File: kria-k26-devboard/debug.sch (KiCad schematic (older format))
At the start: 70 parts, among them J8 USB4105-GF-A, J9 0878311420, Q10 BSS138-7-F, Q11 BSS138-7-F, Q17 DTC014TEBTL, Q9 BSS138-7-F, U28 WE-TVS-82400152, U29 MIC5211-3.3YM6-TR, U30 FT4232HPQ, U31 93LC56CT-IMC, U32 74AVC4T245RSVRG4, U33 74AVC4T245RSVRG4, U34 SN74AVC2T245RSWR, U35 SN74AVC2T245RSWR, U36 NC7WZ07P6X, U54 TPD4E05U06QDQARQ1, Y5 ABM8G-12.000MHZ-18-D2Y-T

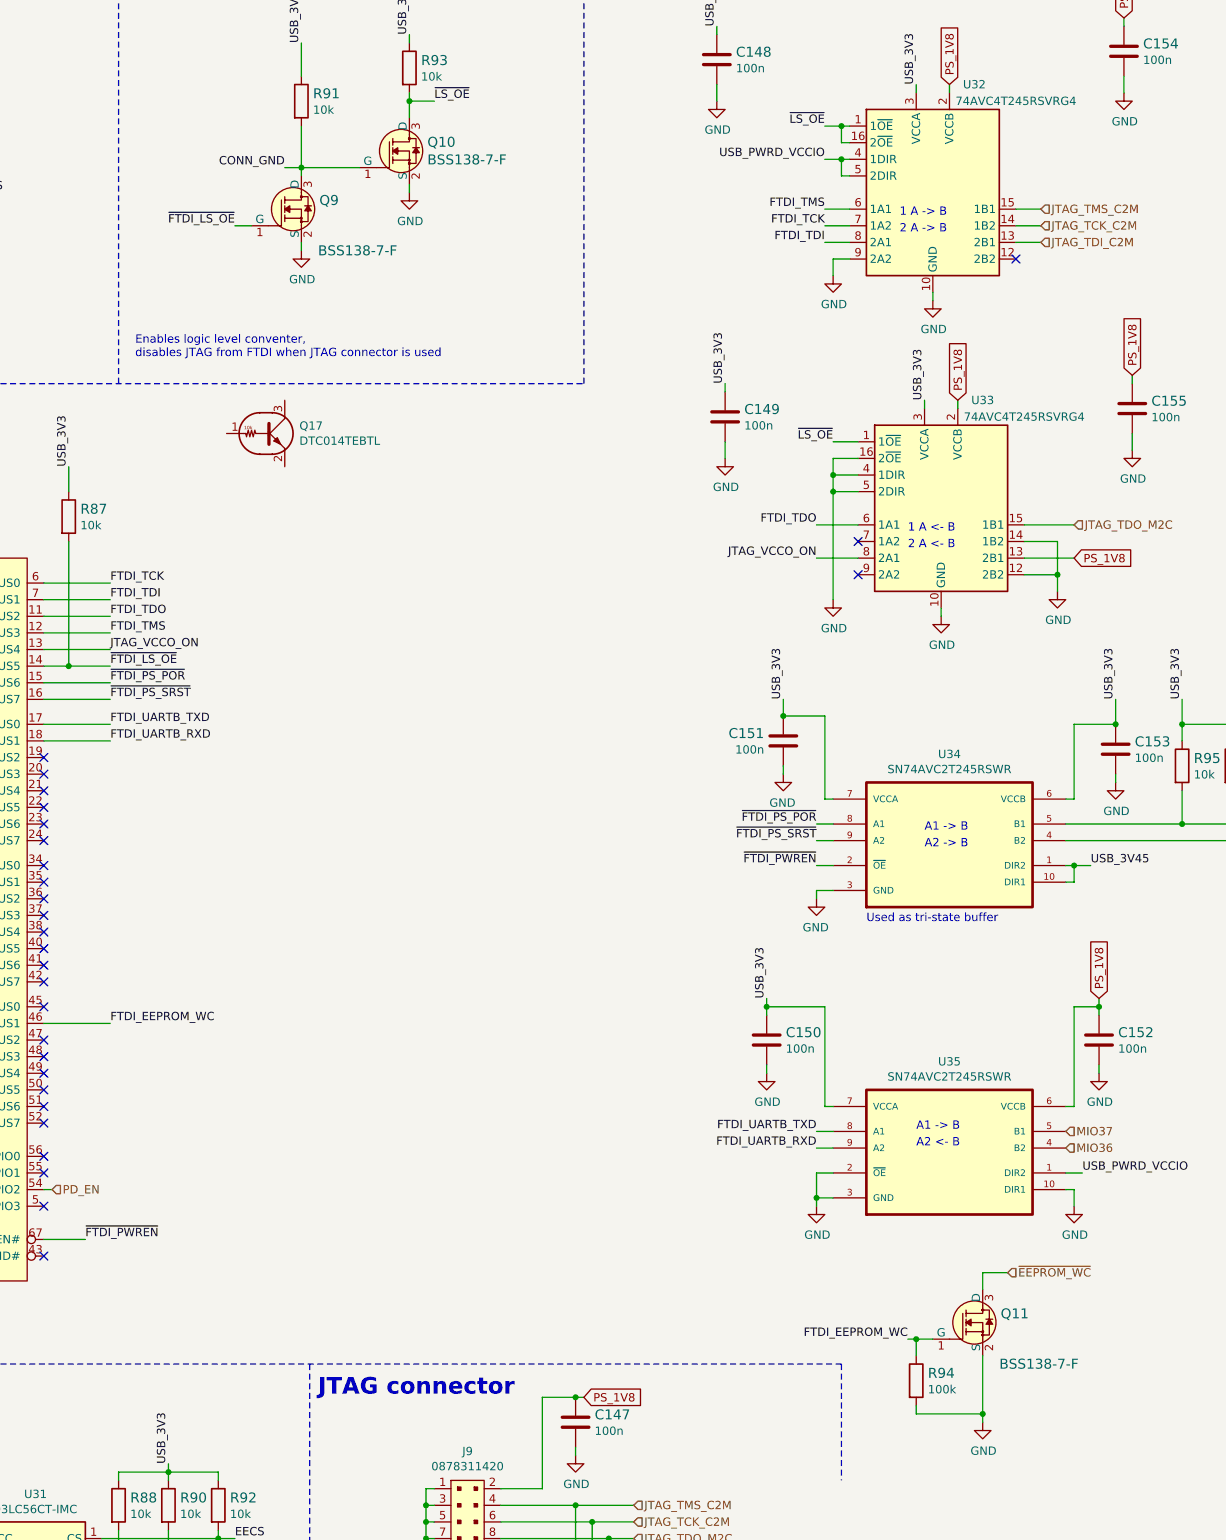
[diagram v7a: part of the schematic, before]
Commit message: Routed PS reset, improved SOM fanout, routed remaing SD 3.0 traces, component size optimization
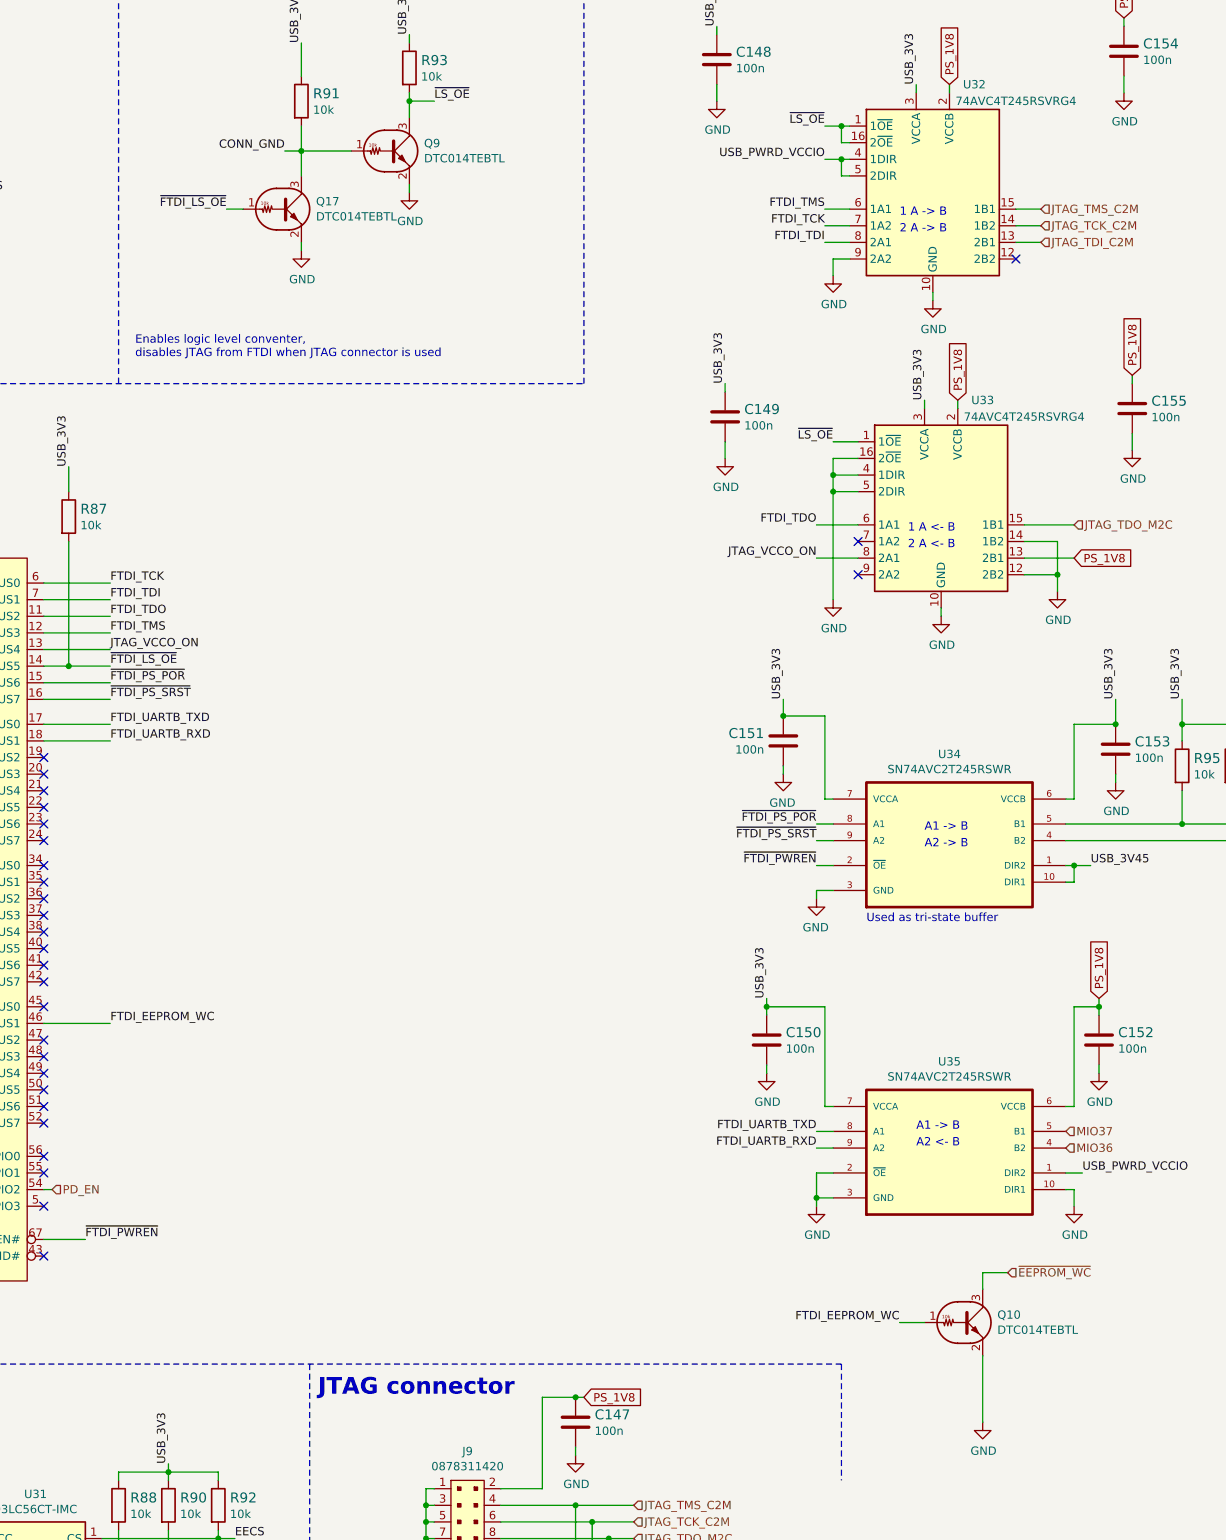
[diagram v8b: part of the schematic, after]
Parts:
- removed Q10, Q11, Q9: BSS138-7-F, antmicro-footprints:SOT-23-3, symbol antmicroTransistorsFETsMOSFETsSingle:BSS138-7-F
- removed R94: R_100k_0402, antmicro-footprints:0402-res, symbol antmicroResistors0402:R_100k_0402
- added Q10, Q9: DTC014TEBTL, antmicro-footprints:SOT-416, symbol antmicroTransistorsBipolarSingle:DTC014TEBTL
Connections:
- net CONN_GND: now also Q17.3 (C), Q9.1 (B)
- net FTDI_EEPROM_WC: now also Q10.1 (B)
- net GND: now also Q17.2 (E), Q10.2 (E), Q9.2 (E)
- net ~EEPROM_WC: now also Q10.3 (C)
- net ~FTDI_LS_OE: now also Q17.1 (B)
- net ~LS_OE: now also Q9.3 (C)
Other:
- moved on the sheet: Q17
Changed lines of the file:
@@
 FTDI_TMS
-$Comp
-L antmicroTransistorsFETsMOSFETsSingle:BSS138-7-F Q9
-U 1 1 623BDEBC
-P 8550 2300
-F 0 "Q9" H 8658 2353 60  0000 L CNN
-F 1 "BSS138-7-F" H 8650 2050 60  0000 L CNN
-F 2 "antmicro-footprints:SOT-23-3" H 8750 2500 60  0001 L CNN
-F 3 "https://www.diodes.com/assets/Datasheets/ds30144.pdf" H 8750 2600 60  0001 L CNN
-F 4 "BSS138-7-F" H 8750 2800 60  0001 L CNN "MPN"
-F 5 "Diodes Incorporated" H 8750 3400 60  0001 L CNN "Manufacturer"
-	1    8550 2300
-	1    0    0    -1
-$EndComp
 $Comp
 L antmicroResistors0402:R_10k_0402 R91
@@
 $EndComp
 $Comp
-L antmicroTransistorsFETsMOSFETsSingle:BSS138-7-F Q10
-U 1 1 623C3158
-P 9200 1950
-F 0 "Q10" H 9308 2003 60  0000 L CNN
-F 1 "BSS138-7-F" H 9308 1897 60  0000 L CNN
-F 2 "antmicro-footprints:SOT-23-3" H 9400 2150 60  0001 L CNN
-F 3 "https://www.diodes.com/assets/Datasheets/ds30144.pdf" H 9400 2250 60  0001 L CNN
-F 4 "BSS138-7-F" H 9400 2450 60  0001 L CNN "MPN"
-F 5 "Diodes Incorporated" H 9400 3050 60  0001 L CNN "Manufacturer"
-	1    9200 1950
-	1    0    0    -1
-$EndComp
-$Comp
 L antmicroResistors0402:R_10k_0402 R93
 U 1 1 623C4098
@@
 $EndComp
 Wire Wire Line
-	8550 2100 8550 2050
+	8550 2100 8550 1950
 Wire Wire Line
 	9200 1750 9200 1650
-Wire Wire Line
-	8550 2050 8900 2050
-Connection ~ 8550 2050
-Wire Wire Line
-	8550 2050 8550 1800
+Connection ~ 8550 1950
+Wire Wire Line
+	8550 1950 8550 1800
 $Comp
 L power:GND #PWR0319
@@
 	9200 1300 9200 1250
 Wire Wire Line
-	8150 2400 8250 2400
-Wire Wire Line
-	8550 2050 8450 2050
+	8100 2300 8200 2300
+Wire Wire Line
+	8550 1950 8450 1950
 Wire Wire Line
 	9200 1650 9350 1650
@@
 Text Label 9350 1650 0    50   ~ 0
 ~LS_OE
-Text Label 8450 2050 2    50   ~ 0
+Text Label 8450 1950 2    50   ~ 0
 CONN_GND
 Wire Wire Line
@@
 JTAG_TDO_M2C
 $Comp
-L antmicroTransistorsFETsMOSFETsSingle:BSS138-7-F Q11
-U 1 1 63AF8DF4
-P 12650 9000
-F 0 "Q11" H 12758 9053 60  0000 L CNN
-F 1 "BSS138-7-F" H 12750 8750 60  0000 L CNN
-F 2 "antmicro-footprints:SOT-23-3" H 12850 9200 60  0001 L CNN
-F 3 "https://www.diodes.com/assets/Datasheets/ds30144.pdf" H 12850 9300 60  0001 L CNN
-F 4 "BSS138-7-F" H 12850 9500 60  0001 L CNN "MPN"
-F 5 "Diodes Incorporated" H 12850 10100 60  0001 L CNN "Manufacturer"
-	1    12650 9000
-	1    0    0    -1
-$EndComp
-$Comp
 L power:GND #PWR0333
 U 1 1 63AF9471
@@
 $EndComp
 Wire Wire Line
-	12250 9100 12350 9100
-Wire Wire Line
 	12650 8700 12650 8800
-Wire Wire Line
-	12250 9500 12250 9550
-Wire Wire Line
-	12250 9550 12650 9550
-Wire Wire Line
-	12650 9550 12650 9600
-Wire Wire Line
-	12250 9200 12250 9100
-Wire Wire Line
-	12650 9200 12650 9550
-Connection ~ 12650 9550
 Wire Wire Line
 	12650 8700 12800 8700
@@
 Text Label 7400 7200 0    50   ~ 0
 FTDI_EEPROM_WC
-Text Label 12200 9100 2    50   ~ 0
+Text Label 12150 9000 2    50   ~ 0
 FTDI_EEPROM_WC
-Wire Wire Line
-	12200 9100 12250 9100
-Connection ~ 12250 9100
 $Comp
 L antmicroRectangularConnectorsHeadersMalePins:0878311420 J9
@@
 Text Label 7400 5050 0    50   ~ 0
 ~FTDI_LS_OE
-Text Label 8150 2400 2    50   ~ 0
+Text Label 8100 2300 2    50   ~ 0
 ~FTDI_LS_OE
 Text Label 4800 1500 0    50   ~ 0
@@
 Wire Wire Line
 	4800 2300 4800 2350
-$Comp
-L antmicroResistors0402:R_100k_0402 R94
-U 1 1 66B3994C
-P 12250 9350
-F 0 "R94" V 12205 9420 60  0000 L CNN
-F 1 "R_100k_0402" H 12250 9200 60  0001 C CNN
-F 2 "antmicro-footprints:0402-res" H 12450 9550 60  0001 L CNN
-F 3 "" H 12250 9350 50  0001 C CNN
-F 4 "VISHAY" H 12450 9750 60  0001 L CNN "Manufacturer"
-F 5 "CRCW0402100KFKEDHP" H 12450 9650 60  0001 L CNN "MPN"
-F 6 "100k" V 12303 9420 50  0000 L CNN "Val"
-	1    12250 9350
-	0    1    1    0
-$EndComp
 Wire Notes Line
 	5600 3350 5600 500
@@
 Text Notes 600  3550 0    100  ~ 20
 Decoupling and Filtering
-Text Notes 7550 3200 0    50   ~ 0
-Enables logic level conventer,\ndisables JTAG from FTDI when JTAG connector is used
 Text HLabel 15450 6200 2    50   Input ~ 0
 ~PS_SRST_C2M
@@
 L antmicroTransistorsBipolarSingle:DTC014TEBTL Q17
 U 1 1 63983E69
-P 8350 3650
-F 0 "Q17" H 8538 3696 50  0000 L CNN
-F 1 "DTC014TEBTL" H 8538 3605 50  0000 L CNN
-F 2 "antmicro-footprints:SOT-416" H 8550 3350 50  0001 L CNN
-F 3 "" H 8350 3650 50  0001 L CNN
-F 4 "ROHM Semiconductor" H 8950 3550 50  0001 C CNN "Manufacturer"
-F 5 "DTC014TEBTL" H 8800 3450 50  0001 C CNN "MPN"
-	1    8350 3650
+P 8450 2300
+F 0 "Q17" H 8638 2346 50  0000 L CNN
+F 1 "DTC014TEBTL" H 8638 2255 50  0000 L CNN
+F 2 "antmicro-footprints:SOT-416" H 8650 2000 50  0001 L CNN
+F 3 "" H 8450 2300 50  0001 L CNN
+F 4 "ROHM Semiconductor" H 9050 2200 50  0001 C CNN "Manufacturer"
+F 5 "DTC014TEBTL" H 8900 2100 50  0001 C CNN "MPN"
+	1    8450 2300
 	1    0    0    -1
 $EndComp
@@
 Wire Wire Line
 	1450 2100 1550 2100
+$Comp
+L antmicroTransistorsBipolarSingle:DTC014TEBTL Q9
+U 1 1 63285C0B
+P 9100 1950
+F 0 "Q9" H 9288 1996 50  0000 L CNN
+F 1 "DTC014TEBTL" H 9288 1905 50  0000 L CNN
+F 2 "antmicro-footprints:SOT-416" H 9300 1650 50  0001 L CNN
+F 3 "" H 9100 1950 50  0001 L CNN
+F 4 "ROHM Semiconductor" H 9700 1850 50  0001 C CNN "Manufacturer"
+F 5 "DTC014TEBTL" H 9550 1750 50  0001 C CNN "MPN"
+	1    9100 1950
+	1    0    0    -1
+$EndComp
+Wire Wire Line
+	8550 1950 8850 1950
+Text Notes 7550 3200 0    50   ~ 0
+Enables logic level conventer,\ndisables JTAG from FTDI when JTAG connector is used
+Wire Wire Line
+	12150 9000 12300 9000
 Wire Bus Line
 	4700 6500 4700 6700
+Wire Wire Line
+	12650 9200 12650 9600
+$Comp
+L antmicroTransistorsBipolarSingle:DTC014TEBTL Q10
+U 1 1 634A6C2F
+P 12550 9000
+F 0 "Q10" H 12738 9046 50  0000 L CNN
+F 1 "DTC014TEBTL" H 12738 8955 50  0000 L CNN
+F 2 "antmicro-footprints:SOT-416" H 12750 8700 50  0001 L CNN
+F 3 "" H 12550 9000 50  0001 L CNN
+F 4 "ROHM Semiconductor" H 13150 8900 50  0001 C CNN "Manufacturer"
+F 5 "DTC014TEBTL" H 13000 8800 50  0001 C CNN "MPN"
+	1    12550 9000
+	1    0    0    -1
+$EndComp
 $EndSCHEMATC
